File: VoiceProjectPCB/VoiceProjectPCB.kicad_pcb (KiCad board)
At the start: 2 copper layers, 83.8 x 73.7 mm, 61 parts, among them J1 Conn_01x02_Socket, J2 Conn_01x02_Socket, J3 217B-CA04, J4 Conn_01x06_Socket, J5 Conn_01x06_Socket, J6 Screw_Terminal_01x02, SW3 SW_Push, SW4 SW_Push, U1 PAM8406D, U2 PAM8406D, U4 ESP32-WROOM-E, U5 AMS1117-3.3, U6 PCM5102A

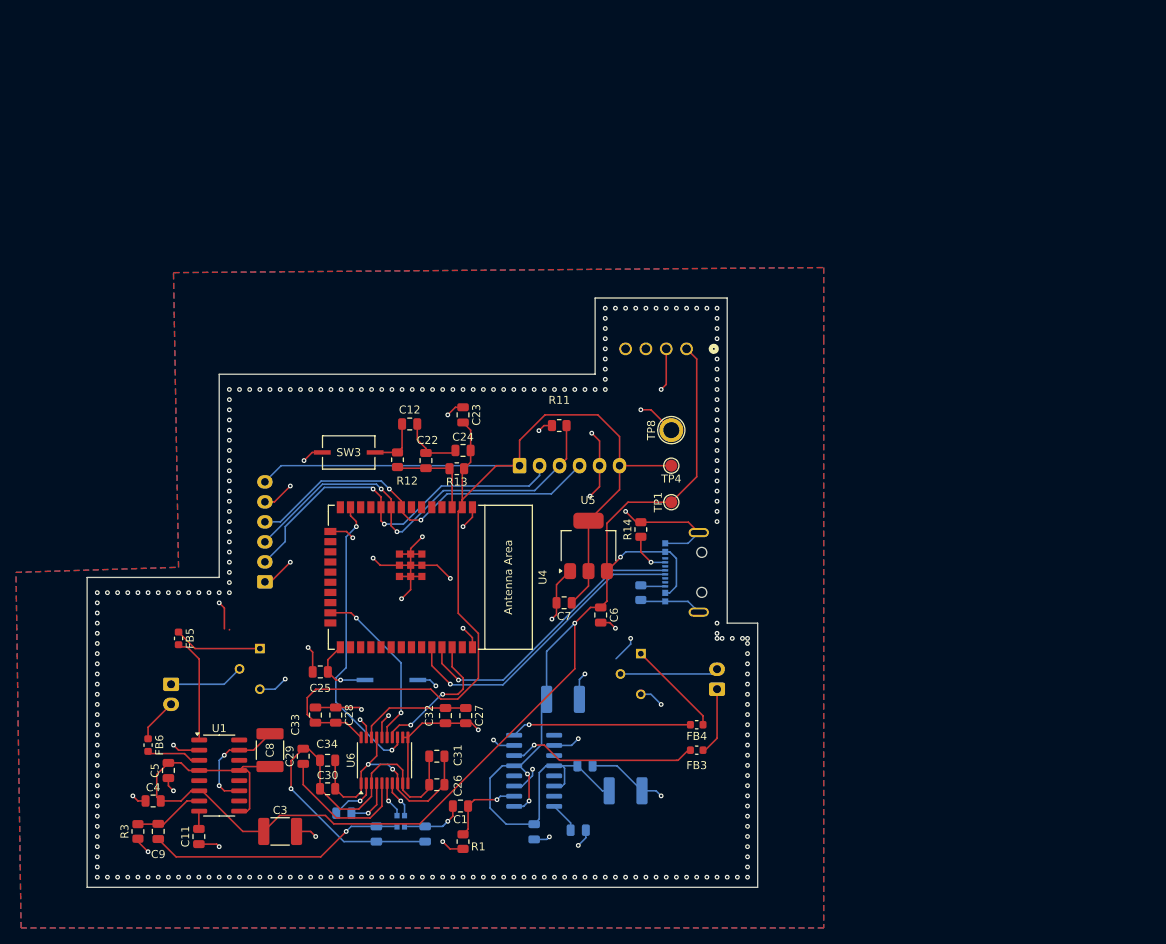
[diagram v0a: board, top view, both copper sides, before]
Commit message: Mk 2 PCB, Switched to DSP for Voice Modulation
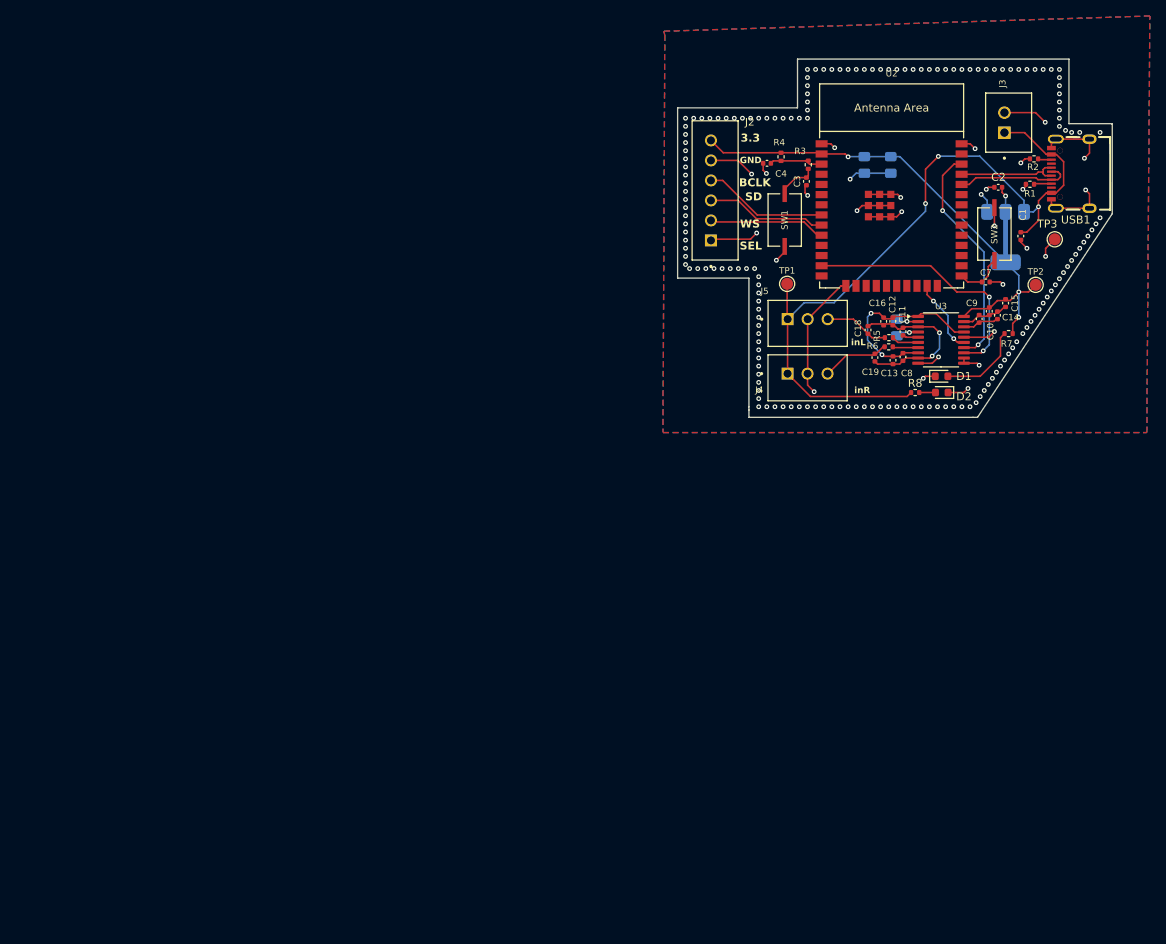
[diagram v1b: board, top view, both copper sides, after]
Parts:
- removed C20: 1uF, Capacitor_SMD:C_0805_2012Metric
- removed C22, C24, C25, C26, C27, C28, C30: 0.1uF, Capacitor_SMD:C_0805_2012Metric
- removed C23: 22uF, Capacitor_SMD:C_0805_2012Metric
- removed C29, C35: 2.2uF, Capacitor_SMD:C_0805_2012Metric
- removed C31, C32, C33, C34: 10uF, Capacitor_SMD:C_0805_2012Metric
- removed C36, C37: 2.2nF, Capacitor_SMD:C_0805_2012Metric
- removed FB3, FB4, FB5, FB6: FerriteBead, Inductor_SMD:L_0603_1608Metric
- removed J1: Conn_01x02_Socket, Connector_JST:JST_EH_B2B-EH-A_1x02_P2.50mm_Vertical
- removed J6: Screw_Terminal_01x02, ScrewTerminal:CONN_1725672_PXC
- removed R11: 100k, Resistor_SMD:R_0805_2012Metric
- removed R12: 0, Resistor_SMD:R_0805_2012Metric
- removed R13: 10k, Resistor_SMD:R_0805_2012Metric
- removed R14, R15: 5.1k, Resistor_SMD:R_0805_2012Metric
- removed RN1: 470, Resistor_SMD:R_Array_Convex_2x0606
- removed RV1, RV2: 10k, 3310P_025_103L:POT_3310P-025-103L
- removed SW3, SW4: SW_Push, Switch:SW2_PTS636 SM25F SMTR LFS_CNK
- removed TP4: TestPoint, TestPoint:TestPoint_Pad_D1.5mm
- removed TP8: TestPoint, TestPoint:TestPoint_Plated_Hole_D2.0mm
- removed U4: ESP32-WROOM-E, Espressif:ESP32-WROOM-32E
- removed U5: AMS1117-3.3, Package_TO_SOT_SMD:SOT-223-3_TabPin2
- removed U6: PCM5102A, Package_SO:TSSOP-20_4.4x6.5mm_P0.65mm
- added C10: 0.1uF, Capacitor_SMD:C_0402_1005Metric, F.Cu at (236.6, 65.8)
- added C13: 10uF, Capacitor_SMD:C_0402_1005Metric, F.Cu at (224.6, 71.9)
- added C18: 2.2nF, Capacitor_SMD:C_0402_1005Metric, F.Cu at (221.4, 68.1)
- added C19: 2.2nF, Capacitor_SMD:C_0402_1005Metric, F.Cu at (222.3, 71.6)
- added C2: 22uF, Capacitor_SMD:C_0402_1005Metric, F.Cu at (237.7, 50.3)
- added D1: 3V, LED_SMD:LED_0603_1608Metric, F.Cu at (230.6, 73.9)
- added D2: LED, LED_SMD:LED_0603_1608Metric, F.Cu at (230.7, 75.9)
- added R2: 5.1k, Resistor_SMD:R_0402_1005Metric, F.Cu at (242.2, 46.7)
- added R4: 10k, Resistor_SMD:R_0402_1005Metric, F.Cu at (210.6, 46.5)
- added R5: 470, Resistor_SMD:R_0402_1005Metric, F.Cu at (224.1, 69.1)
- added R6: 470, Resistor_SMD:R_0402_1005Metric, F.Cu at (224.0, 70.2)
- added R7: 350, Resistor_SMD:R_0402_1005Metric, F.Cu at (239.0, 68.6)
- added R8: 100, Resistor_SMD:R_0402_1005Metric, F.Cu at (227.3, 75.9)
- added SW1: SW_Push, Switch:SW2_PTS636 SM25F SMTR LFS_CNK, F.Cu at (211.0, 54.4)
- added SW2: SW_Push, Switch:SW2_PTS636 SM25F SMTR LFS_CNK, F.Cu at (237.2, 56.1)
- added TP2: TestPoint, TestPoint:TestPoint_Pad_D1.5mm, F.Cu at (242.4, 62.5)
- added TP3: TestPoint, TestPoint:TestPoint_Pad_D1.5mm, F.Cu at (244.8, 56.8)
- added U3: PCM5102A, Package_SO:TSSOP-20_4.4x6.5mm_P0.65mm, F.Cu at (230.6, 69.4)
- added USB1: TYPE-C 16PIN 2MD(073), easyeda2kicad:USB-C-SMD_TYPE-C-6PIN-2MD-073, F.Cu at (246.7, 48.6)
- C1: value 0.1uF -> 10uF; footprint Capacitor_SMD:C_0805_2012Metric -> Capacitor_SMD:C_0402_1005Metric
- C11: value 1uF -> 2.2uF; footprint Capacitor_SMD:C_0805_2012Metric -> Capacitor_SMD:C_0402_1005Metric
- C12, C9: footprint Capacitor_SMD:C_0805_2012Metric -> Capacitor_SMD:C_0402_1005Metric
- C14: value 20uF -> 10uF; footprint Capacitor_SMD:C_1812_4532Metric -> Capacitor_SMD:C_0402_1005Metric; moved to F.Cu
- C15, C16: value 1uF -> 10uF; footprint Capacitor_SMD:C_0805_2012Metric -> Capacitor_SMD:C_0402_1005Metric; moved to F.Cu
- C17: value 20uF -> 2.2uF; footprint Capacitor_SMD:C_1812_4532Metric -> Capacitor_SMD:C_0805_2012Metric_Pad1.18x1.45mm_HandSolder
- C3, C8: value 20uF -> 0.1uF; footprint Capacitor_SMD:C_1812_4532Metric -> Capacitor_SMD:C_0402_1005Metric
- C4: value 1uF -> 0.1uF; footprint Capacitor_SMD:C_0805_2012Metric -> Capacitor_SMD:C_0402_1005Metric
- C5: value 1uF -> 22uF; footprint Capacitor_SMD:C_0805_2012Metric -> Capacitor_SMD:C_0805_2012Metric_Pad1.18x1.45mm_HandSolder; moved to B.Cu
- C6: value 10uF -> 0.1uF; footprint Capacitor_SMD:C_0805_2012Metric -> Capacitor_SMD:C_0805_2012Metric_Pad1.18x1.45mm_HandSolder; moved to B.Cu
- C7: value 22uF -> 0.1uF; footprint Capacitor_SMD:C_0805_2012Metric -> Capacitor_SMD:C_0402_1005Metric
- J2: value Conn_01x02_Socket -> Conn_01x06_Socket; footprint Connector_JST:JST_EH_B2B-EH-A_1x02_P2.50mm_Vertical -> B6B_XH_A:JST_B6B-XH-A; moved to F.Cu
- J3: value 217B-CA04 -> Screw_Terminal_01x02; footprint 217B_CA04 (1):ATTEND_217B-CA04 -> B2B_XH_A:JST_B2B-XH-A; moved to F.Cu
- J4, J5: value Conn_01x06_Socket -> Conn_01x03_Socket; footprint Connector_JST:JST_EH_B6B-EH-A_1x06_P2.50mm_Vertical -> B3B_XH_A:JST_B3B-XH-A; moved to F.Cu
- R1: value 10k -> 5.1k; footprint Resistor_SMD:R_0805_2012Metric -> Resistor_SMD:R_0402_1005Metric
- R3: value 10k -> 0; footprint Resistor_SMD:R_0805_2012Metric -> Resistor_SMD:R_0402_1005Metric
- U1: value PAM8406D -> AMS1117-3.3; footprint Package_SO:SOP-16_3.9x9.9mm_P1.27mm -> Package_TO_SOT_SMD:SOT-223-3_TabPin2; moved to B.Cu
- U2: value PAM8406D -> ESP32-WROOM-E; footprint Package_SO:SOP-16_3.9x9.9mm_P1.27mm -> Espressif:ESP32-WROOM-32E; moved to F.Cu
- moved C9 121.0 mm to (235.3, 66.7), turned to 90 degrees
- moved U1 119.1 mm to (238.6, 56.5), turned to -90 degrees
- moved R3 118.2 mm to (214.0, 47.5), turned to -90 degrees
- moved C5 115.3 mm to (221.0, 47.5)
- moved C4 110.6 mm to (208.8, 47.3), turned to 180 degrees
- moved R1 108.5 mm to (241.7, 49.9), turned to 180 degrees
- moved C11 108.3 mm to (225.8, 68.3)
- moved C3 104.5 mm to (213.7, 49.6), turned to 90 degrees
- moved C1 99.9 mm to (240.5, 56.4), turned to -90 degrees
- moved C8 93.1 mm to (225.8, 71.5)
- moved J2 91.8 mm to (202.3, 50.7)
- moved C15 88.5 mm to (238.6, 64.8), turned to -90 degrees
- moved U2 84.2 mm to (224.4, 51.9), turned to 0 degrees
- moved C14 75.5 mm to (237.6, 66.3), turned to 90 degrees
- moved J4 72.5 mm to (213.9, 74.1), turned to 180 degrees
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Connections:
- C1 pad 1: Net-(U2-INR) -> +5V
- C1 pad 2: /inR -> GND
- C11 pad 1: GND -> /vneg
- C11 pad 2: Net-(U1-VREF) -> GNDA
- C12 pad 1: GND -> GNDA
- C12 pad 2: Net-(C12-Pad2) -> +3.3VA
- C14 pad 1: +5V -> /ldo
- C15 pad 1: GND -> +3.3V
- C15 pad 2: +5V -> GND
- C16 pad 1: GND -> +3.3VA
- C16 pad 2: +5V -> GNDA
- C17 pad 1: +5V -> Net-(U3-CAPP)
- C17 pad 2: GND -> Net-(U3-CAPM)
- C3 pad 1: +5V -> GND
- C3 pad 2: GND -> Net-(C3-Pad2)
- C4 pad 1: GND -> Net-(U2-EN/CHIP_PU)
- C4 pad 2: +5V -> GND
- C5 pad 2: +5V -> +3.3V
- C6 pad 1: +5V -> GND
- C6 pad 2: GND -> +3.3V
- C7 pad 1: +3.3V -> Net-(U2-GPIO0/BOOT/ADC2_CH1)
- C8 pad 1: +5V -> GNDA
- C8 pad 2: GND -> +3.3VA
- C9 pad 1: Net-(U1-INL) -> /ldo
- C9 pad 2: /inL -> GND
- J2 pad 1: Net-(J2-Pin_1) -> GND
- J2 pad 2: Net-(J2-Pin_2) -> /wsIn
- J4 pad 1: GND -> +5V
- J4 pad 2: /wsIn -> GND
- J4 pad 3: /sdIn -> /inR
- J5 pad 1: +3.3V -> +5V
- J5 pad 2: /wsIn -> GND
- J5 pad 3: /sdIn -> /inL
- R1 pad 1: GND -> /cc21
- R1 pad 2: Net-(U2-INR) -> GND
- R3 pad 1: GND -> Net-(U2-EN/CHIP_PU)
- R3 pad 2: Net-(U1-INL) -> Net-(C3-Pad2)
- U1 pad 1: Net-(U1-+OUT_L) -> GND
- U1 pad 2: GND -> +3.3V
- U1 pad 3: Net-(U1--OUT_L) -> +5V
- U2 pad 1: unconnected-(U2-+OUT_L-Pad1) -> GND
- U2 pad 10: Net-(U2-INR) -> /wsIn
- U2 pad 11: GND -> unconnected-(U2-DAC_2/ADC2_CH9/GPIO26-Pad11)
- U2 pad 13: +5V -> /bckOut
- U2 pad 14: Net-(U2--OUT_R) -> unconnected-(U2-MTDI/GPIO12/ADC2_CH5-Pad14)
- U2 pad 16: Net-(U2-+OUT_R) -> unconnected-(U2-MTCK/GPIO13/ADC2_CH4-Pad16)
- U2 pad 2: GND -> +3.3V
- U2 pad 3: unconnected-(U2--OUT_L-Pad3) -> Net-(U2-EN/CHIP_PU)
- U2 pad 4: +5V -> unconnected-(U2-SENSOR_VP/GPIO36/ADC1_CH0-Pad4)
- U2 pad 6: +5V -> unconnected-(U2-GPIO34/ADC1_CH6-Pad6)
- U2 pad 8: Net-(U2-VREF) -> /bckIn
- U2 pad 9: +5V -> /sdIn
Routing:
- net +5V: track 220.6 -> 95.7 mm, vias 4 -> 3
- net GND: track 214.7 -> 110.1 mm, vias 277 -> 193
- net +3.3V: track 158.8 -> 73.5 mm, vias 0 -> 4
- net /sdIn: track 53.4 -> 15.1 mm, vias 2 -> 0
- net /d2-: track 38.2 -> 0.00 mm, vias 1 -> 0
- net GNDA: track 57.7 -> 20.8 mm, vias 1 -> 2
- net /d2+: track 36.5 -> 0.00 mm, vias 1 -> 0
- net /wsIn: track 46.7 -> 14.6 mm, vias 2 -> 0
- net /bckIn: track 47.1 -> 15.6 mm, vias 2 -> 0
- net /inL: track 32.4 -> 8.11 mm, vias 1 -> 0
- net Net-(U2--OUT_R): track 23.6 -> 0.00 mm, vias 1 -> 0
- net Net-(U2-+OUT_R): track 22.3 -> 0.00 mm, vias 1 -> 0
- net /vneg: track 17.6 -> 2.06 mm
- net /d-: track 0.00 -> 14.5 mm
- net Net-(U1-+OUT_L): track 13.3 -> 0.00 mm
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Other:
- board size 83.8 x 73.7 mm -> 54.3 x 44.8 mm
- board text added: "3.3"
- board text added: "BCLK"
- board text added: "GND"
- board text added: "SD"
- board text added: "SEL"
- board text added: "WS"
- board text added: "inL"
- board text added: "inR"
